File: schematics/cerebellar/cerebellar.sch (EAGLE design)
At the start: 67 parts, among them CON2 ODrive1, CON4 Odrive3, CON5 ODrive4, CON6 Odrive2, CON7 ODrive5, CON8 ODrive6, IC3 LTC7001, P1 Foot1, P10 SPI2, P11 Foot2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

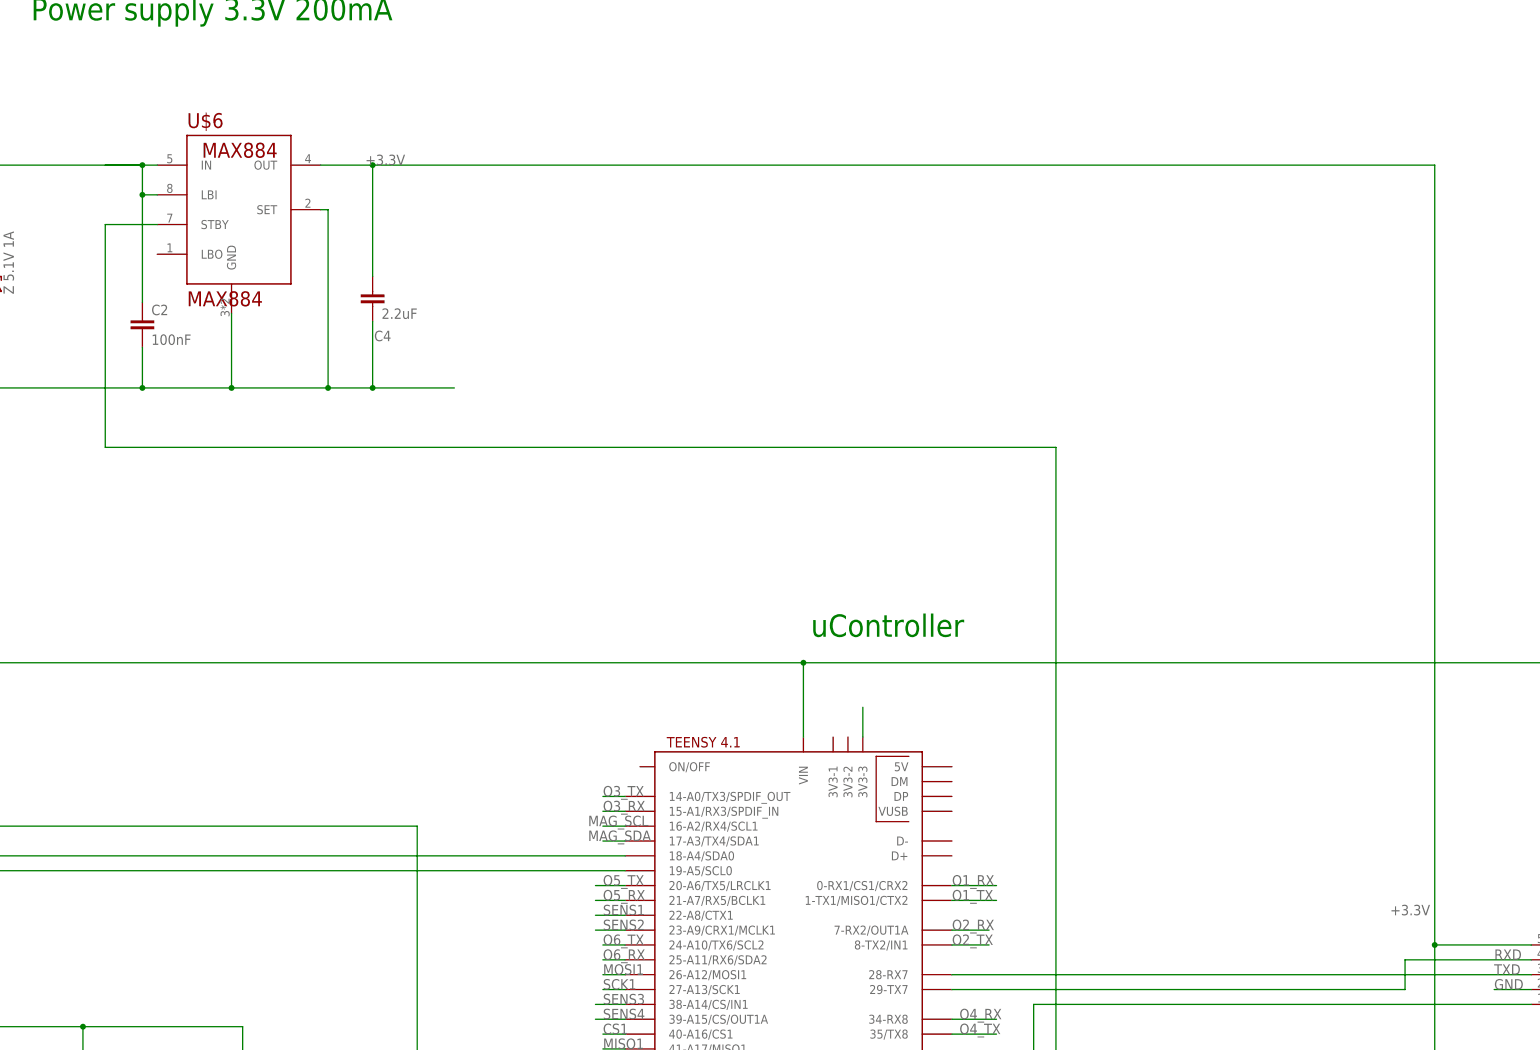
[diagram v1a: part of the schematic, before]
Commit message: Fixed hard iron magnetometer
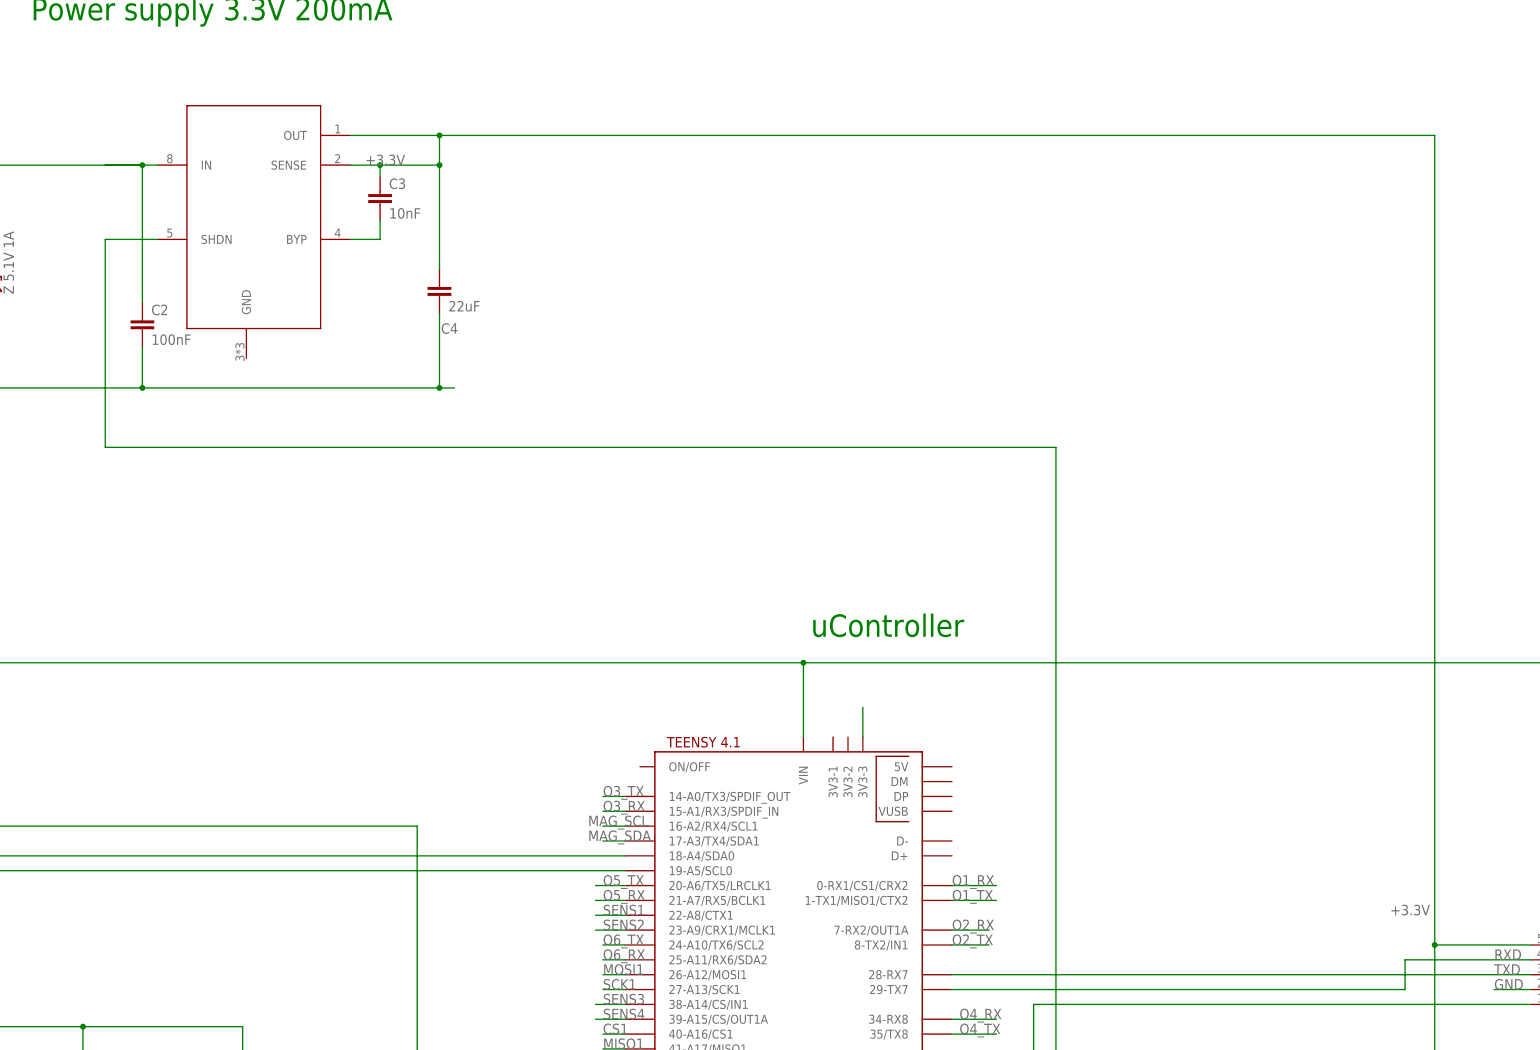
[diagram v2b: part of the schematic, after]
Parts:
- removed U$6: MAX884, MAX884:MAX884
- added C3: 10nF, rcl:C-EU025-025X050
- added U$8: LT1763, LT1763:LT1763
- C4: value 2.2uF -> 22uF
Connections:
- new net N$9: U$1.6-OUT1D, U$8.SHDN
- net +3.3V: now also C3.1, U$8.OUT, U$8.SENSE; no longer U$6.OUT
- net +5V: now also U$8.IN; no longer U$6.IN, U$6.LBI
- net GND: no longer U$6.GND, U$6.SET
- net N$8: now also C3.2, U$8.BYP; no longer U$1.6-OUT1D, U$6.STBY
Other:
- moved on the sheet: C4
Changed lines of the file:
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@@
 <part name="R8" library="rcl" library_urn="urn:adsk.eagle:library:334" deviceset="R-EU_" device="0204/7" package3d_urn="urn:adsk.eagle:package:23498/2" value="1K"/>
 <part name="P17" library="jst-ph" deviceset="JST-PH6" device="" value="MAG"/>
-<part name="U$6" library="MAX884" deviceset="MAX884" device=""/>
 <part name="C2" library="rcl" library_urn="urn:adsk.eagle:library:334" deviceset="C-EU" device="025-025X050" package3d_urn="urn:adsk.eagle:package:23629/2" value="100nF"/>
-<part name="C4" library="rcl" library_urn="urn:adsk.eagle:library:334" deviceset="C-EU" device="025-025X050" package3d_urn="urn:adsk.eagle:package:23629/2" value="2.2uF"/>
+<part name="C4" library="rcl" library_urn="urn:adsk.eagle:library:334" deviceset="C-EU" device="025-025X050" package3d_urn="urn:adsk.eagle:package:23629/2" value="22uF"/>
+<part name="U$8" library="LT1763" deviceset="LT1763" device=""/>
+<part name="C3" library="rcl" library_urn="urn:adsk.eagle:library:334" deviceset="C-EU" device="025-025X050" package3d_urn="urn:adsk.eagle:package:23629/2" value="10nF"/>
 </parts>
 <sheets>
@@
 <attribute name="VALUE" x="259.08" y="25.146" size="1.778" layer="96" rot="R180"/>
 </instance>
-<instance part="U$6" gate="G$1" x="26.67" y="167.64" smashed="yes">
-<attribute name="NAME" x="19.05" y="184.15" size="2.54" layer="94"/>
-<attribute name="VALUE" x="19.05" y="153.67" size="2.54" layer="94"/>
-</instance>
 <instance part="C2" gate="G$1" x="11.43" y="151.765" smashed="yes">
 <attribute name="NAME" x="12.954" y="152.146" size="1.778" layer="95"/>
 <attribute name="VALUE" x="12.954" y="147.066" size="1.778" layer="96"/>
 </instance>
-<instance part="C4" gate="G$1" x="50.8" y="156.21" smashed="yes">
-<attribute name="NAME" x="51.054" y="147.701" size="1.778" layer="95"/>
-<attribute name="VALUE" x="52.324" y="151.511" size="1.778" layer="96"/>
+<instance part="C4" gate="G$1" x="62.23" y="157.48" smashed="yes">
+<attribute name="NAME" x="62.484" y="148.971" size="1.778" layer="95"/>
+<attribute name="VALUE" x="63.754" y="152.781" size="1.778" layer="96"/>
+</instance>
+<instance part="U$8" gate="G$1" x="39.37" y="170.18" smashed="yes"/>
+<instance part="C3" gate="G$1" x="52.07" y="173.355" smashed="yes">
+<attribute name="NAME" x="53.594" y="173.736" size="1.778" layer="95"/>
+<attribute name="VALUE" x="53.594" y="168.656" size="1.778" layer="96"/>
 </instance>
 </instances>
@@
 <junction x="-36.83" y="139.7"/>
 <junction x="-22.86" y="139.7"/>
-<wire x1="64.77" y1="139.7" x2="50.8" y2="139.7" width="0.1524" layer="91"/>
-<wire x1="50.8" y1="139.7" x2="43.18" y2="139.7" width="0.1524" layer="91"/>
-<wire x1="43.18" y1="139.7" x2="26.67" y2="139.7" width="0.1524" layer="91"/>
-<wire x1="26.67" y1="139.7" x2="11.43" y2="139.7" width="0.1524" layer="91"/>
+<wire x1="64.77" y1="139.7" x2="62.23" y2="139.7" width="0.1524" layer="91"/>
+<wire x1="62.23" y1="139.7" x2="11.43" y2="139.7" width="0.1524" layer="91"/>
 <wire x1="11.43" y1="139.7" x2="-13.97" y2="139.7" width="0.1524" layer="91"/>
 <wire x1="-13.97" y1="139.7" x2="-22.86" y2="139.7" width="0.1524" layer="91"/>
@@
 <junction x="-13.97" y="139.7"/>
 <pinref part="D3" gate="G$1" pin="A"/>
-<pinref part="U$6" gate="G$1" pin="GND"/>
-<wire x1="26.67" y1="152.4" x2="26.67" y2="139.7" width="0.1524" layer="91"/>
-<junction x="26.67" y="139.7"/>
 <pinref part="C2" gate="G$1" pin="2"/>
 <wire x1="11.43" y1="146.685" x2="11.43" y2="139.7" width="0.1524" layer="91"/>
 <junction x="11.43" y="139.7"/>
-<pinref part="U$6" gate="G$1" pin="SET"/>
-<wire x1="41.91" y1="170.18" x2="43.18" y2="170.18" width="0.1524" layer="91"/>
-<wire x1="43.18" y1="170.18" x2="43.18" y2="139.7" width="0.1524" layer="91"/>
-<junction x="43.18" y="139.7"/>
-<wire x1="50.8" y1="151.13" x2="50.8" y2="139.7" width="0.1524" layer="91"/>
-<junction x="50.8" y="139.7"/>
+<wire x1="62.23" y1="152.4" x2="62.23" y2="139.7" width="0.1524" layer="91"/>
+<junction x="62.23" y="139.7"/>
 <pinref part="C4" gate="G$1" pin="2"/>
 </segment>
@@
 <junction x="-13.97" y="177.8"/>
 <pinref part="D3" gate="G$1" pin="C"/>
-<pinref part="U$6" gate="G$1" pin="IN"/>
 <wire x1="-13.97" y1="177.8" x2="11.43" y2="177.8" width="0.1524" layer="91"/>
-<pinref part="U$6" gate="G$1" pin="LBI"/>
 <wire x1="11.43" y1="177.8" x2="5.08" y2="177.8" width="0.1524" layer="91"/>
 <wire x1="11.43" y1="177.8" x2="13.97" y2="177.8" width="0.1524" layer="91"/>
-<wire x1="13.97" y1="172.72" x2="11.43" y2="172.72" width="0.1524" layer="91"/>
-<wire x1="11.43" y1="172.72" x2="11.43" y2="177.8" width="0.1524" layer="91"/>
 <junction x="11.43" y="177.8"/>
 <pinref part="C2" gate="G$1" pin="1"/>
-<wire x1="11.43" y1="172.72" x2="11.43" y2="154.305" width="0.1524" layer="91"/>
-<junction x="11.43" y="172.72"/>
+<wire x1="11.43" y1="177.8" x2="11.43" y2="154.305" width="0.1524" layer="91"/>
+<pinref part="U$8" gate="G$1" pin="IN"/>
 </segment>
 <segment>
@@
 <pinref part="P17" gate="A" pin="5"/>
 <label x="224.79" y="49.53" size="1.778" layer="95"/>
-<pinref part="U$6" gate="G$1" pin="OUT"/>
-<wire x1="41.91" y1="177.8" x2="50.8" y2="177.8" width="0.1524" layer="91"/>
 <label x="49.53" y="177.8" size="1.778" layer="95"/>
-<wire x1="50.8" y1="177.8" x2="50.8" y2="158.75" width="0.1524" layer="91"/>
-<wire x1="50.8" y1="177.8" x2="232.41" y2="177.8" width="0.1524" layer="91"/>
-<junction x="50.8" y="177.8"/>
+<wire x1="62.23" y1="182.88" x2="62.23" y2="177.8" width="0.1524" layer="91"/>
+<wire x1="62.23" y1="177.8" x2="62.23" y2="160.02" width="0.1524" layer="91"/>
+<wire x1="62.23" y1="182.88" x2="232.41" y2="182.88" width="0.1524" layer="91"/>
 <pinref part="P1" gate="G$1" pin="2"/>
 <wire x1="238.76" y1="-96.52" x2="238.76" y2="-91.44" width="0.1524" layer="91"/>
@@
 <pinref part="C4" gate="G$1" pin="1"/>
 <wire x1="232.41" y1="17.78" x2="232.41" y2="44.45" width="0.1524" layer="91"/>
-<wire x1="232.41" y1="44.45" x2="232.41" y2="177.8" width="0.1524" layer="91"/>
+<wire x1="232.41" y1="44.45" x2="232.41" y2="182.88" width="0.1524" layer="91"/>
 <wire x1="232.41" y1="17.78" x2="232.41" y2="-91.44" width="0.1524" layer="91"/>
 <wire x1="232.41" y1="-91.44" x2="238.76" y2="-91.44" width="0.1524" layer="91"/>
@@
 <wire x1="248.92" y1="44.45" x2="232.41" y2="44.45" width="0.1524" layer="91"/>
 <junction x="232.41" y="44.45"/>
-</segment>
-</net>
-<net name="N$8" class="0">
-<segment>
-<pinref part="U$1" gate="G$1" pin="6-OUT1D"/>
-<wire x1="149.86" y1="6.35" x2="167.64" y2="6.35" width="0.1524" layer="91"/>
-<wire x1="167.64" y1="6.35" x2="167.64" y2="129.54" width="0.1524" layer="91"/>
-<wire x1="167.64" y1="129.54" x2="5.08" y2="129.54" width="0.1524" layer="91"/>
-<pinref part="U$6" gate="G$1" pin="STBY"/>
-<wire x1="5.08" y1="129.54" x2="5.08" y2="167.64" width="0.1524" layer="91"/>
-<wire x1="5.08" y1="167.64" x2="13.97" y2="167.64" width="0.1524" layer="91"/>
+<pinref part="U$8" gate="G$1" pin="OUT"/>
+<wire x1="46.99" y1="182.88" x2="62.23" y2="182.88" width="0.1524" layer="91"/>
+<junction x="62.23" y="182.88"/>
+<pinref part="U$8" gate="G$1" pin="SENSE"/>
+<wire x1="46.99" y1="177.8" x2="52.07" y2="177.8" width="0.1524" layer="91"/>
+<junction x="62.23" y="177.8"/>
+<pinref part="C3" gate="G$1" pin="1"/>
+<wire x1="52.07" y1="177.8" x2="62.23" y2="177.8" width="0.1524" layer="91"/>
+<wire x1="52.07" y1="175.895" x2="52.07" y2="177.8" width="0.1524" layer="91"/>
+<junction x="52.07" y="177.8"/>
 </segment>
 </net>
@@
 </segment>
 </net>
+<net name="N$9" class="0">
+<segment>
+<pinref part="U$1" gate="G$1" pin="6-OUT1D"/>
+<wire x1="149.86" y1="6.35" x2="167.64" y2="6.35" width="0.1524" layer="91"/>
+<wire x1="167.64" y1="6.35" x2="167.64" y2="129.54" width="0.1524" layer="91"/>
+<wire x1="5.08" y1="129.54" x2="5.08" y2="165.1" width="0.1524" layer="91"/>
+<wire x1="5.08" y1="129.54" x2="167.64" y2="129.54" width="0.1524" layer="91"/>
+<pinref part="U$8" gate="G$1" pin="SHDN"/>
+<wire x1="13.97" y1="165.1" x2="5.08" y2="165.1" width="0.1524" layer="91"/>
+</segment>
+</net>
+<net name="N$8" class="0">
+<segment>
+<pinref part="C3" gate="G$1" pin="2"/>
+<wire x1="52.07" y1="168.275" x2="52.07" y2="165.1" width="0.1524" layer="91"/>
+<pinref part="U$8" gate="G$1" pin="BYP"/>
+<wire x1="52.07" y1="165.1" x2="46.99" y2="165.1" width="0.1524" layer="91"/>
+</segment>
+</net>

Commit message: new power supply
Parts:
- removed P17: MAG, jst-ph:JST-PH6
- added P16: MAG, jst-ph:JST-PH5
- R20: value 100k -> 25k
- R8: value 1K -> 100
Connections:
- net +3.3V: now also P16.2; no longer P17.5
- net GND: now also P16.3; no longer P17.6
- net MAG_EN: no longer P17.2
- net MAG_INT: now also P16.1; no longer P17.1
- net MAG_SCL: now also P16.4; no longer P17.3
- net MAG_SDA: now also P16.5; no longer P17.4
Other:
- note added: "Power supply 3.3V 500mA"
- note removed: "Power supply 3.3V 200mA"
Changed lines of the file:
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@@
 <part name="L2" library="rcl" library_urn="urn:adsk.eagle:library:334" deviceset="L-EU" device="IRF-3" package3d_urn="urn:adsk.eagle:package:23536/1" value="10uH"/>
 <part name="U$7" library="TLF50211EL" deviceset="TLF50211EL" device=""/>
-<part name="R20" library="rcl" library_urn="urn:adsk.eagle:library:334" deviceset="R-EU_" device="0204/7" package3d_urn="urn:adsk.eagle:package:23498/2" value="100k"/>
+<part name="R20" library="rcl" library_urn="urn:adsk.eagle:library:334" deviceset="R-EU_" device="0204/7" package3d_urn="urn:adsk.eagle:package:23498/2" value="25k"/>
 <part name="R21" library="rcl" library_urn="urn:adsk.eagle:library:334" deviceset="R-EU_" device="0204/7" package3d_urn="urn:adsk.eagle:package:23498/2" value="100k"/>
 <part name="D3" library="diode" library_urn="urn:adsk.eagle:library:210" deviceset="ZENER-DIODE" device="DO41Z10" package3d_urn="urn:adsk.eagle:package:43341/1" value="Z 5.1V 1A"/>
@@
 <part name="R1" library="rcl" library_urn="urn:adsk.eagle:library:334" deviceset="R-EU_" device="0204/7" package3d_urn="urn:adsk.eagle:package:23498/2" value="6.8k"/>
 <part name="P4" library="jst-ph" deviceset="JST-PH2" device="" value="LED"/>
-<part name="R8" library="rcl" library_urn="urn:adsk.eagle:library:334" deviceset="R-EU_" device="0204/7" package3d_urn="urn:adsk.eagle:package:23498/2" value="1K"/>
-<part name="P17" library="jst-ph" deviceset="JST-PH6" device="" value="MAG"/>
+<part name="R8" library="rcl" library_urn="urn:adsk.eagle:library:334" deviceset="R-EU_" device="0204/7" package3d_urn="urn:adsk.eagle:package:23498/2" value="100"/>
 <part name="C2" library="rcl" library_urn="urn:adsk.eagle:library:334" deviceset="C-EU" device="025-025X050" package3d_urn="urn:adsk.eagle:package:23629/2" value="100nF"/>
 <part name="C4" library="rcl" library_urn="urn:adsk.eagle:library:334" deviceset="C-EU" device="025-025X050" package3d_urn="urn:adsk.eagle:package:23629/2" value="22uF"/>
 <part name="U$8" library="LT1763" deviceset="LT1763" device=""/>
 <part name="C3" library="rcl" library_urn="urn:adsk.eagle:library:334" deviceset="C-EU" device="025-025X050" package3d_urn="urn:adsk.eagle:package:23629/2" value="10nF"/>
+<part name="P16" library="jst-ph" deviceset="JST-PH5" device="" value="MAG"/>
 </parts>
 <sheets>
@@
 <text x="125.73" y="97.155" size="3.81" layer="91" distance="80">uController</text>
 <text x="295.91" y="107.315" size="3.81" layer="91" distance="80">PWM LED, 2A</text>
-<text x="-7.62" y="202.565" size="3.81" layer="91" distance="80">Power supply 3.3V 200mA</text>
+<text x="-7.62" y="202.565" size="3.81" layer="91" distance="80">Power supply 3.3V 500mA</text>
 </plain>
 <instances>
@@
 <attribute name="VALUE" x="342.9" y="89.408" size="1.778" layer="96"/>
 </instance>
-<instance part="P17" gate="A" x="256.54" y="12.7" smashed="yes" rot="R180">
-<attribute name="NAME" x="259.08" y="4.318" size="1.778" layer="95" rot="R180"/>
-<attribute name="VALUE" x="259.08" y="25.146" size="1.778" layer="96" rot="R180"/>
-</instance>
 <instance part="C2" gate="G$1" x="11.43" y="151.765" smashed="yes">
 <attribute name="NAME" x="12.954" y="152.146" size="1.778" layer="95"/>
@@
 <attribute name="NAME" x="53.594" y="173.736" size="1.778" layer="95"/>
 <attribute name="VALUE" x="53.594" y="168.656" size="1.778" layer="96"/>
+</instance>
+<instance part="P16" gate="G$1" x="256.54" y="10.16" smashed="yes" rot="R180">
+<attribute name="NAME" x="259.08" y="4.318" size="1.778" layer="95" rot="R180"/>
+<attribute name="VALUE" x="259.08" y="22.606" size="1.778" layer="96" rot="R180"/>
 </instance>
 </instances>
@@
 </segment>
 <segment>
-<wire x1="248.92" y1="20.32" x2="243.84" y2="20.32" width="0.1524" layer="91"/>
-<label x="243.84" y="20.32" size="1.778" layer="95"/>
-<pinref part="P17" gate="A" pin="6"/>
-</segment>
-<segment>
 <pinref part="P14" gate="G$1" pin="2"/>
 <wire x1="248.92" y1="36.83" x2="242.57" y2="36.83" width="0.1524" layer="91"/>
 <label x="242.57" y="36.83" size="1.778" layer="95"/>
+</segment>
+<segment>
+<wire x1="248.92" y1="12.7" x2="234.95" y2="12.7" width="0.1524" layer="91"/>
+<label x="234.95" y="12.7" size="1.778" layer="95"/>
+<pinref part="P16" gate="G$1" pin="3"/>
 </segment>
 </net>
@@
 </segment>
 <segment>
-<wire x1="248.92" y1="12.7" x2="228.6" y2="12.7" width="0.1524" layer="91"/>
-<label x="234.95" y="12.7" size="1.778" layer="95"/>
-<pinref part="P17" gate="A" pin="3"/>
+<wire x1="248.92" y1="15.24" x2="234.95" y2="15.24" width="0.1524" layer="91"/>
+<label x="234.95" y="15.24" size="1.778" layer="95"/>
+<pinref part="P16" gate="G$1" pin="4"/>
 </segment>
 </net>
@@
 </segment>
 <segment>
-<wire x1="248.92" y1="15.24" x2="227.33" y2="15.24" width="0.1524" layer="91"/>
-<label x="234.95" y="15.24" size="1.778" layer="95"/>
-<pinref part="P17" gate="A" pin="4"/>
+<wire x1="248.92" y1="17.78" x2="234.95" y2="17.78" width="0.1524" layer="91"/>
+<label x="234.95" y="17.78" size="1.778" layer="95"/>
+<pinref part="P16" gate="G$1" pin="5"/>
 </segment>
 </net>
 <net name="MAG_EN" class="0">
-<segment>
-<wire x1="248.92" y1="10.16" x2="229.87" y2="10.16" width="0.1524" layer="91"/>
-<label x="234.95" y="10.16" size="1.778" layer="95"/>
-<pinref part="P17" gate="A" pin="2"/>
-</segment>
 <segment>
 <pinref part="U$1" gate="G$1" pin="9-OUT1C"/>
@@
 </segment>
 <segment>
-<pinref part="P17" gate="A" pin="1"/>
 <wire x1="248.92" y1="7.62" x2="229.87" y2="7.62" width="0.1524" layer="91"/>
 <label x="234.95" y="7.62" size="1.778" layer="95"/>
+<pinref part="P16" gate="G$1" pin="1"/>
 </segment>
 </net>
@@
 <net name="+3.3V" class="0">
 <segment>
-<wire x1="248.92" y1="17.78" x2="232.41" y2="17.78" width="0.1524" layer="91"/>
-<pinref part="P17" gate="A" pin="5"/>
 <label x="224.79" y="49.53" size="1.778" layer="95"/>
 <label x="49.53" y="177.8" size="1.778" layer="95"/>
@@
 <junction x="238.76" y="-91.44"/>
 <pinref part="C4" gate="G$1" pin="1"/>
-<wire x1="232.41" y1="17.78" x2="232.41" y2="44.45" width="0.1524" layer="91"/>
 <wire x1="232.41" y1="44.45" x2="232.41" y2="182.88" width="0.1524" layer="91"/>
-<wire x1="232.41" y1="17.78" x2="232.41" y2="-91.44" width="0.1524" layer="91"/>
+<wire x1="232.41" y1="44.45" x2="232.41" y2="10.16" width="0.1524" layer="91"/>
+<wire x1="232.41" y1="10.16" x2="232.41" y2="-91.44" width="0.1524" layer="91"/>
 <wire x1="232.41" y1="-91.44" x2="238.76" y2="-91.44" width="0.1524" layer="91"/>
-<junction x="232.41" y="17.78"/>
 <pinref part="P14" gate="G$1" pin="5"/>
 <wire x1="248.92" y1="44.45" x2="232.41" y2="44.45" width="0.1524" layer="91"/>
@@
 <wire x1="52.07" y1="175.895" x2="52.07" y2="177.8" width="0.1524" layer="91"/>
 <junction x="52.07" y="177.8"/>
-</segment>
-</net>
+<wire x1="248.92" y1="10.16" x2="232.41" y2="10.16" width="0.1524" layer="91"/>
+<junction x="232.41" y="10.16"/>
+<pinref part="P16" gate="G$1" pin="2"/>
+</segment>
+</net>
